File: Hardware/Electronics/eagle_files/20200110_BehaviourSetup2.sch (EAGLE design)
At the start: 21 parts, among them Q1 IRF540, Q2 IRF540, Q3 IRF540

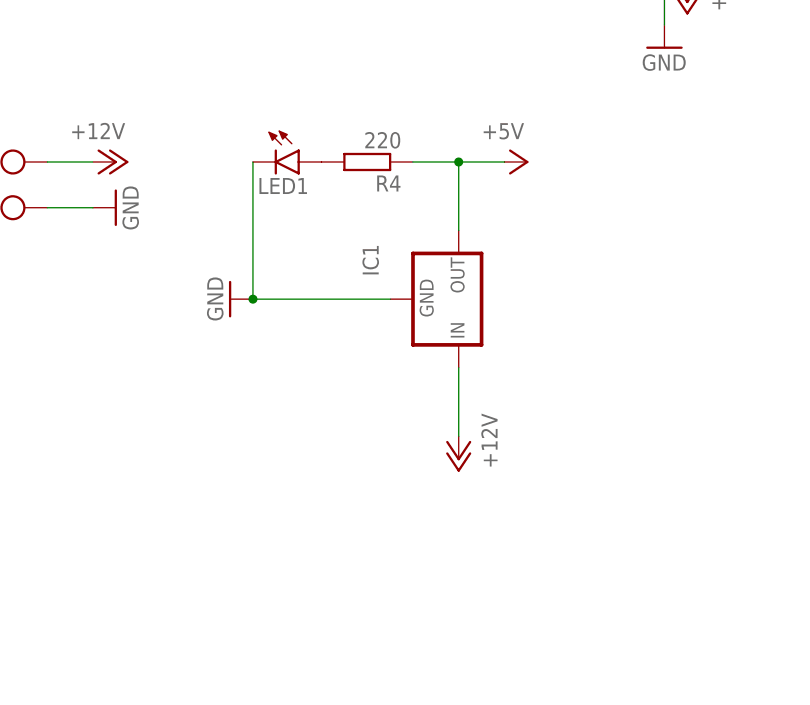
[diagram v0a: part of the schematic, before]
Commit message: updated schematics to include correct power converter
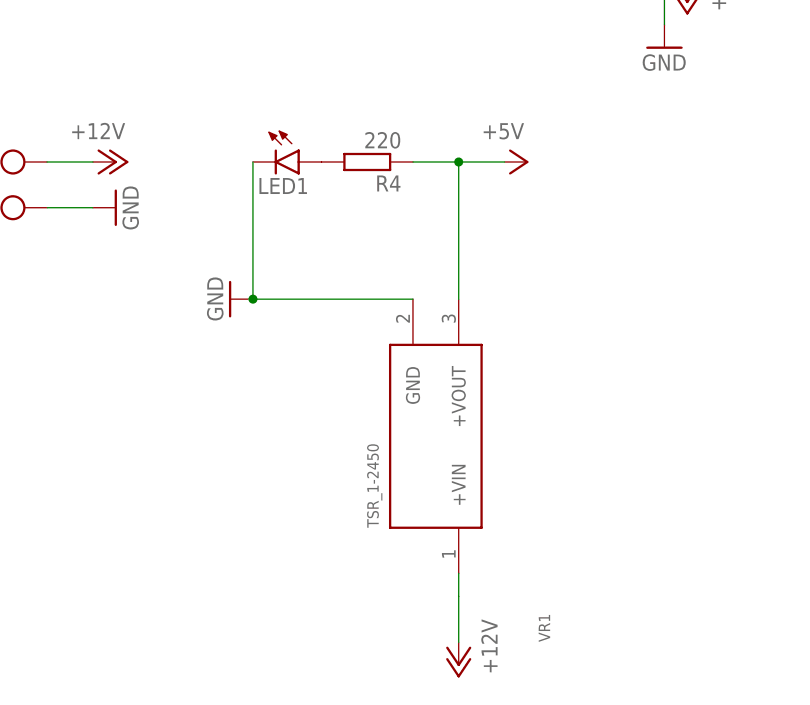
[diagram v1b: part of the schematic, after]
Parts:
- removed IC1: (no value), v-reg:79XXS
- added VR1: TSR_1-2450, TSR_1-2450:TSR_1-2450
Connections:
- net +12V: now also VR1.+VIN; no longer IC1.IN
- net +5V: now also VR1.+VOUT; no longer IC1.OUT
- net GND: now also VR1.GND; no longer IC1.GND
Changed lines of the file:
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@@
 <part name="P+4" library="supply1" library_urn="urn:adsk.eagle:library:371" deviceset="+12V" device=""/>
 <part name="GND4" library="supply1" library_urn="urn:adsk.eagle:library:371" deviceset="GND" device=""/>
-<part name="IC1" library="v-reg" library_urn="urn:adsk.eagle:library:409" deviceset="79XXS" device="" package3d_urn="urn:adsk.eagle:package:30343/1"/>
 <part name="P+5" library="supply1" library_urn="urn:adsk.eagle:library:371" deviceset="+12V" device=""/>
 <part name="GND5" library="supply1" library_urn="urn:adsk.eagle:library:371" deviceset="GND" device=""/>
@@
 <part name="P+9" library="supply1" library_urn="urn:adsk.eagle:library:371" deviceset="+12V" device=""/>
 <part name="D1" library="diode" library_urn="urn:adsk.eagle:library:210" deviceset="1N4004" device="" package3d_urn="urn:adsk.eagle:package:43336/1"/>
+<part name="VR1" library="TSR_1-2450" deviceset="TSR_1-2450" device=""/>
 </parts>
 <sheets>
@@
 <attribute name="VALUE" x="38.1" y="2.54" size="1.778" layer="96"/>
 </instance>
-<instance part="IC1" gate="1" x="17.78" y="-22.86" smashed="yes" rot="R90">
-<attribute name="NAME" x="8.89" y="-20.32" size="1.778" layer="95" rot="R90"/>
-<attribute name="VALUE" x="11.43" y="-20.32" size="1.778" layer="96" rot="R90"/>
-</instance>
-<instance part="P+5" gate="1" x="17.78" y="-40.64" smashed="yes" rot="R180">
-<attribute name="VALUE" x="20.32" y="-35.56" size="1.778" layer="96" rot="R270"/>
+<instance part="P+5" gate="1" x="17.78" y="-63.5" smashed="yes" rot="R180">
+<attribute name="VALUE" x="20.32" y="-58.42" size="1.778" layer="96" rot="R270"/>
 </instance>
 <instance part="GND5" gate="1" x="-7.62" y="-22.86" smashed="yes" rot="R270">
@@
 <attribute name="NAME" x="76.2" y="104.6226" size="1.778" layer="95"/>
 <attribute name="VALUE" x="76.2" y="101.8286" size="1.778" layer="96"/>
+</instance>
+<instance part="VR1" gate="G$1" x="15.24" y="-38.1" smashed="yes" rot="MR90">
+<attribute name="NAME" x="26.67" y="-60.96" size="1.27" layer="95" rot="MR90"/>
+<attribute name="VALUE" x="8.89" y="-48.26" size="1.27" layer="96" rot="MR90" align="top-left"/>
 </instance>
 </instances>
@@
 <pinref part="GND5" gate="1" pin="GND"/>
 <wire x1="-5.08" y1="-7.62" x2="-5.08" y2="-22.86" width="0.1524" layer="91"/>
-<pinref part="IC1" gate="1" pin="GND"/>
-<wire x1="-5.08" y1="-22.86" x2="10.16" y2="-22.86" width="0.1524" layer="91"/>
+<wire x1="-5.08" y1="-22.86" x2="12.7" y2="-22.86" width="0.1524" layer="91"/>
 <junction x="-5.08" y="-22.86"/>
+<pinref part="VR1" gate="G$1" pin="GND"/>
 </segment>
 <segment>
@@
 </segment>
 <segment>
-<pinref part="IC1" gate="1" pin="IN"/>
 <pinref part="P+5" gate="1" pin="+12V"/>
-<wire x1="17.78" y1="-30.48" x2="17.78" y2="-38.1" width="0.1524" layer="91"/>
+<pinref part="VR1" gate="G$1" pin="+VIN"/>
+<wire x1="17.78" y1="-55.88" x2="17.78" y2="-60.96" width="0.1524" layer="91"/>
+<wire x1="17.78" y1="-55.88" x2="17.78" y2="-53.34" width="0.1524" layer="91"/>
 </segment>
 <segment>
@@
 <segment>
 <pinref part="R4" gate="G$1" pin="1"/>
-<pinref part="IC1" gate="1" pin="OUT"/>
 <wire x1="12.7" y1="-7.62" x2="17.78" y2="-7.62" width="0.1524" layer="91"/>
-<wire x1="17.78" y1="-7.62" x2="17.78" y2="-15.24" width="0.1524" layer="91"/>
 <pinref part="P+6" gate="1" pin="+5V"/>
 <wire x1="22.86" y1="-7.62" x2="17.78" y2="-7.62" width="0.1524" layer="91"/>
 <junction x="17.78" y="-7.62"/>
-</segment>
-<segment>
+<pinref part="VR1" gate="G$1" pin="+VOUT"/>
+<wire x1="17.78" y1="-7.62" x2="17.78" y2="-22.86" width="0.1524" layer="91"/>
+</segment>
+<segment>

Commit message: Changed circuitry, rebuilt PCB
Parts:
- added D2, D3: 1N4004, diode:1N4004
- C1: device rcl:CPOL-EUE3.5-10 -> rcl:CPOL-EUE5-8.5
- X1, X2, X3: value (none) -> 22-23-2021; device con-molex:KK-156-2 -> con-molex:22-23-2021
- X4, X5, X6: value (none) -> 22-23-2031; device con-molex:KK-156-3 -> con-molex:22-23-2031
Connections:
- removed net N$2: Q1.D, X1-1.S
- removed net N$8: ARDUINO_NANO1.D4, R6.2, X4-3.S, X5-3.S
- removed net N$9: X4-2.S, X5-2.S
- new net N$12: D2.A, Q2.D, X2-1.S
- new net N$13: D1.A, Q1.D, X1-1.S
- net +12V: now also D1.C, D2.C
- net +5V: now also D3.C; no longer D1.C
- net GND: now also X4-2.S, X5-2.S
- net N$10: now also ARDUINO_NANO1.D4; no longer ARDUINO_NANO1.D2
- net N$4: now also ARDUINO_NANO1.D2, R6.2, X4-3.S, X5-3.S; no longer Q2.D, X2-1.S
- net N$6: now also D3.A; no longer D1.A
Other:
- moved on the sheet: D1, R6
